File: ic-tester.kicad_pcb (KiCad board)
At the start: 2 copper layers, 91.4 x 68.6 mm, 16 parts, among them IC1 MCP23017-E_SP, IC2 MCP23017-E_SP, IC3 MCP23017-E_SP, J1 Conn_01x04, SW1 SW_SPST

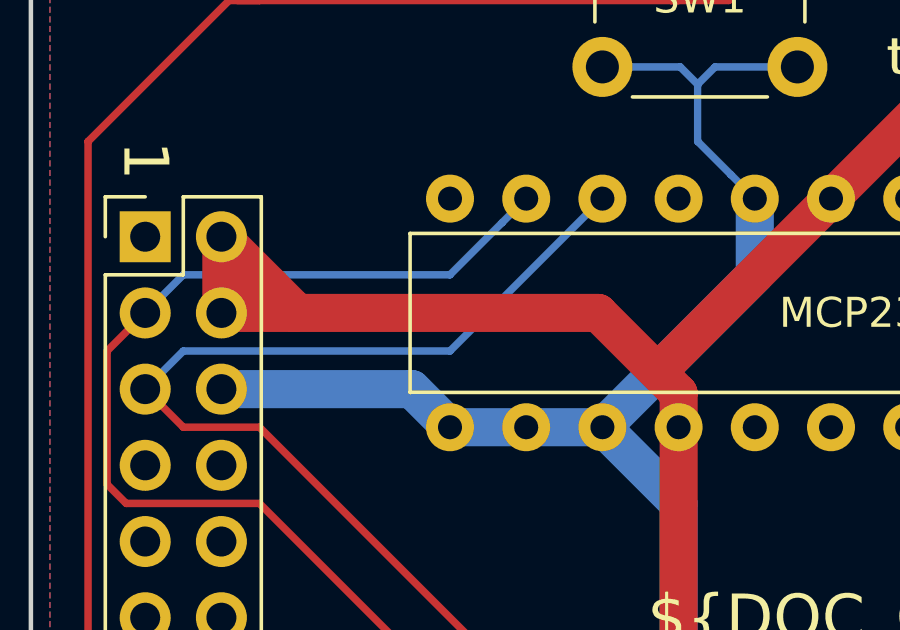
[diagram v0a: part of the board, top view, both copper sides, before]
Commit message: Draft of software for the tester.
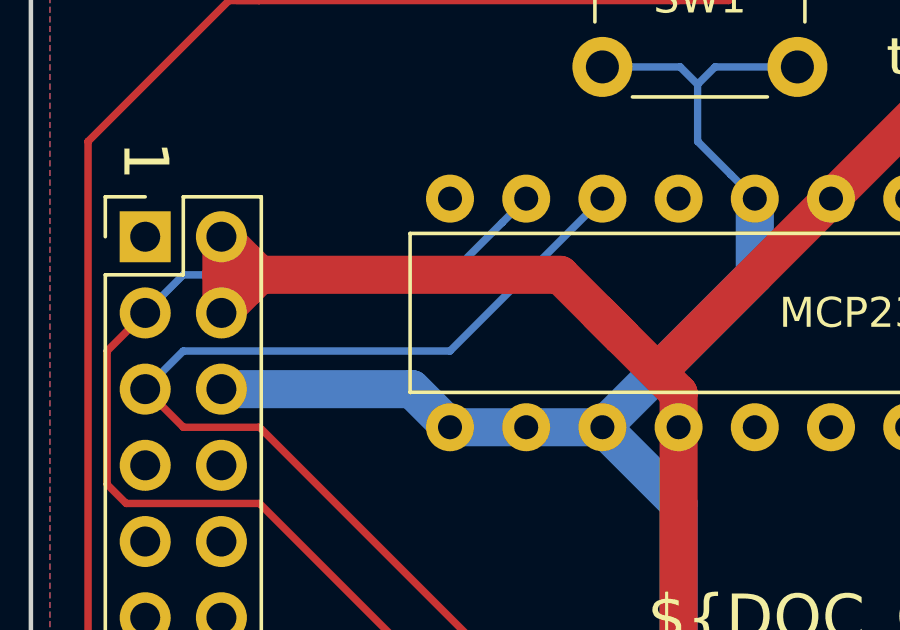
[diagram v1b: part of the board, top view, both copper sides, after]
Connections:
- net Net-(IC3-Pad24) renamed /SW_TEST
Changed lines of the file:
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@@
     (thickness 1.6)
     (drawings 24)
-    (tracks 394)
+    (tracks 396)
     (zones 0)
     (modules 16)
@@
   (net 82 /GPIO1)
   (net 83 /GPIO4)
-  (net 84 "Net-(IC3-Pad24)")
+  (net 84 /SW_TEST)
   (net_class Default "This is the default net class."
     (clearance 0.2)
@@
     (add_net /SCL)
     (add_net /SDA)
+    (add_net /SW_TEST)
     (add_net /ZIF01)
     (add_net /ZIF02)
@@
     (add_net "Net-(D3-Pad2)")
     (add_net "Net-(D4-Pad2)")
-    (add_net "Net-(IC3-Pad24)")
     (add_net "Net-(J_RASPI1-Pad1)")
     (add_net "Net-(J_RASPI1-Pad10)")
@@
       (net 70 GND))
     (pad 1 thru_hole circle (at 0 0 90) (size 2 2) (drill 1.1) (layers *.Cu *.Mask)
-      (net 84 "Net-(IC3-Pad24)"))
+      (net 84 /SW_TEST))
     (pad 2 thru_hole circle (at 6.5 4.5 90) (size 2 2) (drill 1.1) (layers *.Cu *.Mask)
       (net 70 GND))
     (pad 1 thru_hole circle (at 6.5 0 90) (size 2 2) (drill 1.1) (layers *.Cu *.Mask)
-      (net 84 "Net-(IC3-Pad24)"))
+      (net 84 /SW_TEST))
     (model ${KISYS3DMOD}/Button_Switch_THT.3dshapes/SW_PUSH_6mm_H13mm.wrl
       (at (xyz 0 0 0))
@@
       (net 70 GND))
     (pad 24 thru_hole oval (at 7.62 10.16 270) (size 1.6 1.6) (drill 0.8) (layers *.Cu *.Mask)
-      (net 84 "Net-(IC3-Pad24)"))
+      (net 84 /SW_TEST))
     (pad "" thru_hole oval (at 0 25.4 270) (size 1.6 1.6) (drill 0.8) (layers *.Cu *.Mask))
     (pad 25 thru_hole oval (at 7.62 7.62 270) (size 1.6 1.6) (drill 0.8) (layers *.Cu *.Mask)
@@
   (segment (start 47.625 64.135) (end 42.545 69.215) (width 1.27) (layer F.Cu) (net 69) (status 20))
   (segment (start 47.625 61.595) (end 47.625 64.135) (width 1.27) (layer F.Cu) (net 69) (status 10))
-  (segment (start 27.305 45.085) (end 27.305 42.545) (width 1.27) (layer F.Cu) (net 69) (status 30))
   (segment (start 47.625 41.275) (end 41.91 46.99) (width 1.27) (layer F.Cu) (net 69) (status 10))
   (segment (start 55.245 33.655) (end 47.625 41.275) (width 1.27) (layer F.Cu) (net 69) (status 20))
-  (segment (start 29.718 44.958) (end 29.718 45.085) (width 1.27) (layer F.Cu) (net 69))
-  (segment (start 39.86637 45.085) (end 29.718 45.085) (width 1.27) (layer F.Cu) (net 69))
-  (segment (start 29.718 45.085) (end 27.305 45.085) (width 1.27) (layer F.Cu) (net 69) (status 20))
-  (segment (start 28.194 44.196) (end 27.305 45.085) (width 1.27) (layer F.Cu) (net 69) (status 20))
-  (segment (start 28.956 44.196) (end 28.194 44.196) (width 1.27) (layer F.Cu) (net 69))
-  (segment (start 28.956 44.196) (end 29.718 44.958) (width 1.27) (layer F.Cu) (net 69))
-  (segment (start 27.305 42.545) (end 28.956 44.196) (width 1.27) (layer F.Cu) (net 69) (status 10))
-  (segment (start 42.545 47.76363) (end 39.86637 45.085) (width 1.27) (layer F.Cu) (net 69))
   (segment (start 42.545 48.895) (end 42.545 47.76363) (width 1.27) (layer F.Cu) (net 69) (status 10))
   (segment (start 102.87 33.655) (end 55.245 33.655) (width 1.27) (layer F.Cu) (net 69))
@@
   (segment (start 34.925 69.215) (end 38.735 73.025) (width 1.27) (layer F.Cu) (net 69))
   (segment (start 42.545 69.215) (end 38.735 73.025) (width 1.27) (layer F.Cu) (net 69))
+  (segment (start 38.59637 43.815) (end 40.64 45.85863) (width 1.27) (layer F.Cu) (net 69))
+  (segment (start 40.64 45.85863) (end 39.86637 45.085) (width 1.27) (layer F.Cu) (net 69))
+  (segment (start 42.545 47.76363) (end 40.64 45.85863) (width 1.27) (layer F.Cu) (net 69))
+  (segment (start 27.305 43.815) (end 27.305 42.545) (width 1.27) (layer F.Cu) (net 69))
+  (segment (start 27.305 45.085) (end 27.305 43.815) (width 1.27) (layer F.Cu) (net 69))
+  (segment (start 28.154999 43.394999) (end 28.575 43.815) (width 1.27) (layer F.Cu) (net 69))
+  (segment (start 27.305 42.545) (end 28.154999 43.394999) (width 1.27) (layer F.Cu) (net 69))
+  (segment (start 27.305 43.815) (end 28.575 43.815) (width 1.27) (layer F.Cu) (net 69))
+  (segment (start 28.575 43.815) (end 38.59637 43.815) (width 1.27) (layer F.Cu) (net 69))
+  (segment (start 28.154999 44.235001) (end 28.575 43.815) (width 1.27) (layer F.Cu) (net 69))
+  (segment (start 27.305 45.085) (end 28.154999 44.235001) (width 1.27) (layer F.Cu) (net 69))
   (segment (start 34.925 89.535) (end 31.115 93.345) (width 1.27) (layer B.Cu) (net 70) (status 10))
   (segment (start 40.005 89.535) (end 36.195 93.345) (width 1.27) (layer B.Cu) (net 70) (status 10))

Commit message: Draft of version 2.0
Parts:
- added K1: FINDER-34.51, Relay_THT:Relay_SPDT_Finder_34.51_Vertical, F.Cu at (-9.40, 40.9)
- added Q1: BC547, Package_TO_SOT_THT:TO-92_Inline, F.Cu at (5.66, 59.3)
- added Q2: BC547, Package_TO_SOT_THT:TO-92_Inline, F.Cu at (11.2, 54.5)
- added Q3: BS250, Package_TO_SOT_THT:TO-92_Inline, F.Cu at (11.2, 59.3)
- added Q4: BS250, Package_TO_SOT_THT:TO-92_Inline, F.Cu at (5.66, 54.5)
- added Q5: BS250, Package_TO_SOT_THT:TO-92_Inline, F.Cu at (-13.1, 47.7)
- R1: value 330 -> 20k
